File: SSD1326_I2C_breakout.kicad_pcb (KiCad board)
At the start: 2 copper layers, 55.9 x 12.8 mm, 24 parts, among them J1 Conn_01x04, U1 MAX607ESA-T, U2 ER-OLED018-1, U3 APX803, U4 AP2112K-3.3

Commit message: adding images and such
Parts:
- removed REF**: ER-OLED018-1_screen, onigaku:ER-OLED018-1_screen
- J1: footprint Connector_PinSocket_2.54mm:PinSocket_1x04_P2.54mm_Vertical -> onigaku:PinSocket_1x04_P2.54mm_Vertical
- renumbered Ce to C8
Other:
- board size 55.9 x 12.8 mm -> 55.7 x 12.8 mm

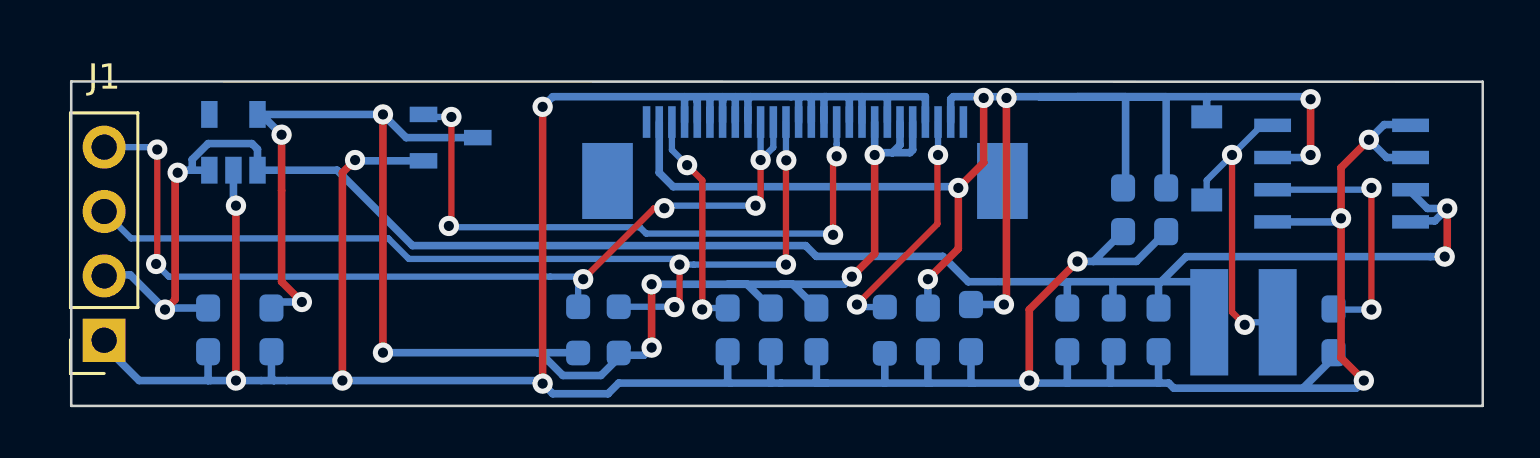
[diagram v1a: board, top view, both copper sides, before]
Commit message: swapped out max607 for a max8570 due to cost savings and obsoletion, using B0520LW schottky due to similar circumstances
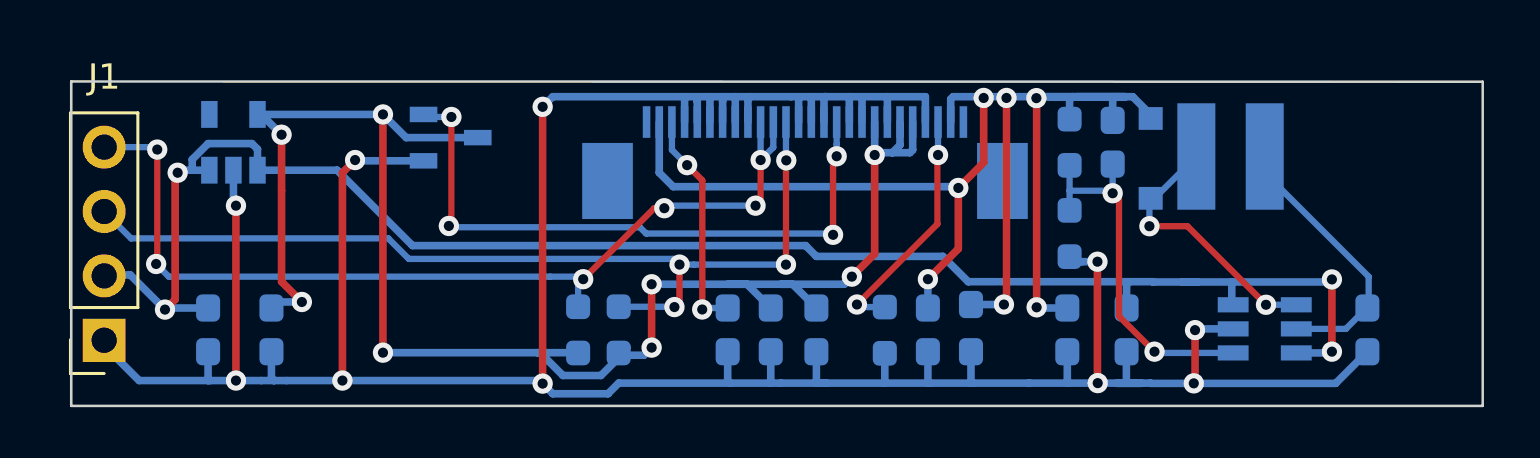
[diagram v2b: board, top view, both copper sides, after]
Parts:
- removed C4: 0.68uF, Capacitor_SMD:C_0603_1608Metric_Pad1.08x0.95mm_HandSolder
- removed C6: 10n, Capacitor_SMD:C_0603_1608Metric_Pad1.08x0.95mm_HandSolder
- removed U1: MAX607ESA-T, onigaku:max607esa&plus_T
- added R4: 88k, Resistor_SMD:R_0603_1608Metric_Pad0.98x0.95mm_HandSolder, B.Cu at (108.2, 30.1)
- added R5: 10k, Resistor_SMD:R_0603_1608Metric_Pad0.98x0.95mm_HandSolder, B.Cu at (108.2, 33.7)
- added U5: MAX8570EUT, onigaku:MAX8570EUT+SOT95P280X145-6N, B.Cu at (115.9, 37.5)
- C1: value 0.68uF -> 4.7uF
- C2: value 0.68uF -> 10pF
- C5: value 0.68uF -> 1uF
- D1: value MBR0520LT1G -> ‎B0520LW-7-F‎; footprint onigaku:MBR0520LT1G -> onigaku:B0520LW
- moved C1 9.25 mm to (120.0, 37.5)
- moved L1 6.56 mm to (114.5, 30.6), turned to 180 degrees
- moved C2 2.70 mm to (109.9, 30.1)
- moved D1 2.21 mm to (111.4, 30.7)
- moved C5 1.26 mm to (110.5, 37.5)
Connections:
- C1 pad 1: +12V -> Net-(C1-Pad1)
- C2 pad 2: GND -> Net-(C2-Pad2)
- C3 pad 1: +5V -> +12V
- L1 pad 1: +5V -> Net-(C1-Pad1)
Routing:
- net GND: track 153.3 -> 133.6 mm, vias 11 -> 10
- net Net-(C2-Pad2): track 0.00 -> 14.6 mm, vias 0 -> 2
- net Net-(C1-Pad1): track 0.00 -> 11.3 mm
- net Net-(C6-Pad1): track 10.2 -> 0.00 mm, vias 2 -> 0
- net +5V: track 76.1 -> 67.5 mm
- net +12V: track 66.6 -> 58.7 mm
- net Net-(D1-Pad2): track 12.5 -> 10.7 mm

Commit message: slimming down to 12mm
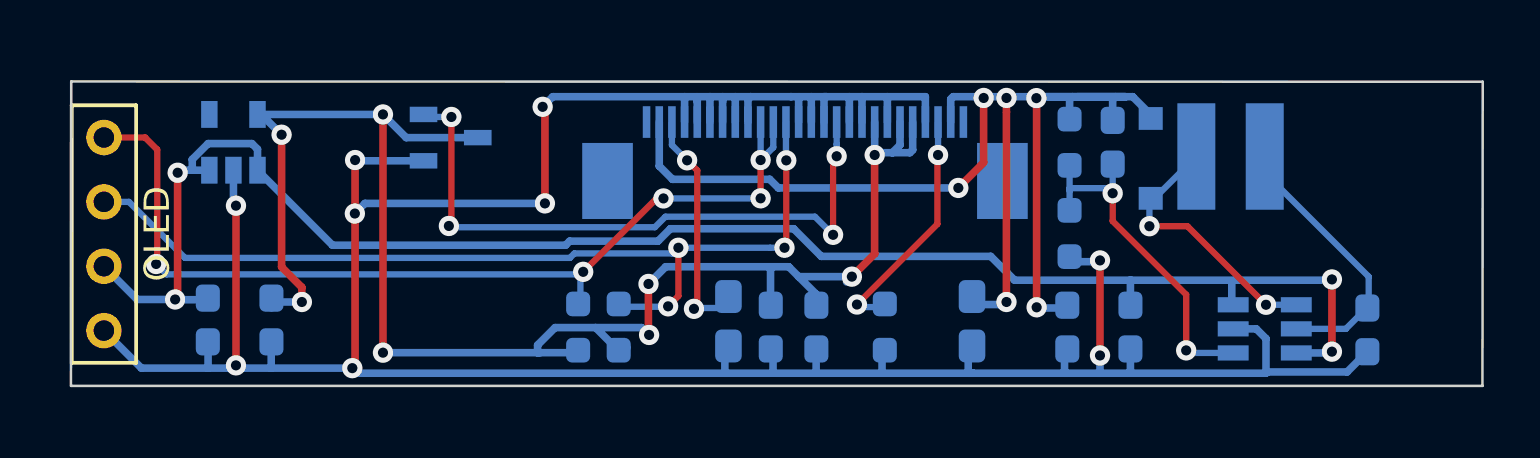
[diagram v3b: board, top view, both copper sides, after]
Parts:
- removed C7, C9: 4.7uF, Capacitor_SMD:C_0603_1608Metric_Pad1.08x0.95mm_HandSolder
- removed C8: 0.1uF, Capacitor_SMD:C_0603_1608Metric_Pad1.08x0.95mm_HandSolder
- added C4: 4.7uF, Capacitor_Tantalum_SMD:CP_EIA-2012-15_AVX-P_Pad1.30x1.05mm_HandSolder, B.Cu at (104.3, 37.1)
- added C6: 4.7uF, Capacitor_Tantalum_SMD:CP_EIA-2012-15_AVX-P_Pad1.30x1.05mm_HandSolder, B.Cu at (94.7, 37.1)
- C10: value 4.7uF -> 0.1uF
- J1: footprint onigaku:PinSocket_1x04_P2.54mm_Vertical -> kbd:OLED
- R4: value 88k -> 82k
- U3: value APX803 -> APX803S; footprint onigaku:APX803-SOT91P240X110-3N -> onigaku:APX803S-SA-SOT91P240X110-3N
- moved C12 0.39 mm to (74.2, 37.1)
- moved C13 0.39 mm to (76.7, 37.1)
- moved J1 0.38 mm to (70.1, 29.9), turned to 270 degrees
- moved C5 0.19 mm to (110.6, 37.4)
- moved R3 0.12 mm to (100.9, 37.4)
- moved C10 0.11 mm to (98.2, 37.4)
- moved C11 0.11 mm to (96.4, 37.4)
- moved C3 0.11 mm to (108.1, 37.4)
- moved R1 0.11 mm to (90.4, 37.4)
- moved R2 0.11 mm to (88.8, 37.4)
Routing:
- net GND: track 133.6 -> 127.2 mm, vias 10 -> 9
- net +12V: track 58.7 -> 53.3 mm, vias 7 -> 6
- net +3V3: track 66.7 -> 67.8 mm
- net Net-(C2-Pad2): track 14.6 -> 13.9 mm
- net SDA: track 38.1 -> 38.6 mm, vias 6 -> 5
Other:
- board size 55.7 x 12.8 mm -> 55.7 x 12 mm

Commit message: moved some stuff over
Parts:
- removed J1: Conn_01x04, kbd:OLED
- added Jee: Conn_01x04, kbd:OLED, F.Cu at (69.3, 29.9)
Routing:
- net SCL: track 37.4 -> 38.1 mm
- net +5V: track 67.0 -> 67.6 mm
- net GND: track 127.2 -> 127.8 mm
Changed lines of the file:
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@@
     (thickness 1.6)
     (drawings 6)
-    (tracks 353)
+    (tracks 354)
     (zones 0)
     (modules 22)
@@
   )
   (module kbd:OLED (layer F.Cu)
-    (at 70.1 29.9 270)
+    (at 69.35 29.9 270)
     (descr "Connecteur 6 pins")
     (tags "CONN DEV")
-    (fp_text reference J1 (at 3.7 2.1 270) (layer F.Fab)
+    (fp_text reference Jee (at 3.7 2.1 270) (layer F.Fab)
       (effects (font (size 0.8128 0.8128) (thickness 0.15)))
     )
     (fp_text value Conn_01x04 (at 3.6 3.3 90) (layer F.SilkS) hide
       (effects (font (size 0.8128 0.8128) (thickness 0.15)))
-    )
-    (fp_text user OLED (at 3.75 -2.1 90) (layer B.SilkS)
-      (effects (font (size 1 1) (thickness 0.15)) (justify mirror))
-    )
-    (fp_text user OLED (at 3.8 -2.1 90) (layer F.SilkS)
-      (effects (font (size 1 1) (thickness 0.15)))
     )
     (fp_line (start -1.27 -1.27) (end 8.89 -1.27) (layer B.SilkS) (width 0.15))
@@
     (fp_line (start 8.89 -1.27) (end 8.89 1.27) (layer F.SilkS) (width 0.15))
     (fp_line (start -1.27 1.27) (end -1.27 -1.27) (layer F.SilkS) (width 0.15))
+    (fp_text user OLED (at 3.75 -2.1 90) (layer B.SilkS)
+      (effects (font (size 1 1) (thickness 0.15)) (justify mirror))
+    )
+    (fp_text user OLED (at 3.8 -2.1 90) (layer F.SilkS)
+      (effects (font (size 1 1) (thickness 0.15)))
+    )
     (pad 4 thru_hole circle (at 7.62 0 270) (size 1.397 1.397) (drill 0.8128) (layers *.Cu *.Mask F.SilkS)
       (net 1 GND))
@@
     )
   )
-  (dimension 55.69 (width 0.15) (layer Dwgs.User)
-    (gr_text "55.690 mm" (at 96.655 25.2) (layer Dwgs.User)
+  (dimension 26 (width 0.15) (layer Dwgs.User)
+    (gr_text "26.000 mm" (at 84.75 24.85) (layer Dwgs.User)
       (effects (font (size 1 1) (thickness 0.15)))
     )
-    (feature1 (pts (xy 124.5 27.69) (xy 124.5 25.913579)))
-    (feature2 (pts (xy 68.81 27.69) (xy 68.81 25.913579)))
-    (crossbar (pts (xy 68.81 26.5) (xy 124.5 26.5)))
-    (arrow1a (pts (xy 124.5 26.5) (xy 123.373496 27.086421)))
-    (arrow1b (pts (xy 124.5 26.5) (xy 123.373496 25.913579)))
-    (arrow2a (pts (xy 68.81 26.5) (xy 69.936504 27.086421)))
-    (arrow2b (pts (xy 68.81 26.5) (xy 69.936504 25.913579)))
-  )
-  (dimension 12 (width 0.15) (layer Dwgs.User)
-    (gr_text "12.000 mm" (at 62.3 33.69 270) (layer Dwgs.User)
+    (feature1 (pts (xy 97.75 27.7) (xy 97.75 25.563579)))
+    (feature2 (pts (xy 71.75 27.7) (xy 71.75 25.563579)))
+    (crossbar (pts (xy 71.75 26.15) (xy 97.75 26.15)))
+    (arrow1a (pts (xy 97.75 26.15) (xy 96.623496 26.736421)))
+    (arrow1b (pts (xy 97.75 26.15) (xy 96.623496 25.563579)))
+    (arrow2a (pts (xy 71.75 26.15) (xy 72.876504 26.736421)))
+    (arrow2b (pts (xy 71.75 26.15) (xy 72.876504 25.563579)))
+  )
+  (dimension 52 (width 0.15) (layer Dwgs.User)
+    (gr_text "52.000 mm" (at 97.75 21.000001) (layer Dwgs.User)
       (effects (font (size 1 1) (thickness 0.15)))
     )
-    (feature1 (pts (xy 68.81 39.69) (xy 63.013579 39.69)))
-    (feature2 (pts (xy 68.81 27.69) (xy 63.013579 27.69)))
-    (crossbar (pts (xy 63.6 27.69) (xy 63.6 39.69)))
-    (arrow1a (pts (xy 63.6 39.69) (xy 63.013579 38.563496)))
-    (arrow1b (pts (xy 63.6 39.69) (xy 64.186421 38.563496)))
-    (arrow2a (pts (xy 63.6 27.69) (xy 63.013579 28.816504)))
-    (arrow2b (pts (xy 63.6 27.69) (xy 64.186421 28.816504)))
-  )
-  (gr_line (start 124.5 27.7) (end 68.81 27.69) (layer Edge.Cuts) (width 0.1))
-  (gr_line (start 124.49 39.7) (end 124.5 27.7) (layer Edge.Cuts) (width 0.1))
-  (gr_line (start 68.8 39.7) (end 124.49 39.7) (layer Edge.Cuts) (width 0.1))
-  (gr_line (start 68.81 27.69) (end 68.8 39.7) (layer Edge.Cuts) (width 0.1))
+    (feature1 (pts (xy 71.75 27.7) (xy 71.75 21.71358)))
+    (feature2 (pts (xy 123.75 27.7) (xy 123.75 21.71358)))
+    (crossbar (pts (xy 123.75 22.300001) (xy 71.75 22.300001)))
+    (arrow1a (pts (xy 71.75 22.300001) (xy 72.876504 21.71358)))
+    (arrow1b (pts (xy 71.75 22.300001) (xy 72.876504 22.886422)))
+    (arrow2a (pts (xy 123.75 22.300001) (xy 122.623496 21.71358)))
+    (arrow2b (pts (xy 123.75 22.300001) (xy 122.623496 22.886422)))
+  )
+  (gr_line (start 123.75 27.7) (end 68.06 27.69) (layer Edge.Cuts) (width 0.1))
+  (gr_line (start 123.74 39.7) (end 123.75 27.7) (layer Edge.Cuts) (width 0.1))
+  (gr_line (start 68.05 39.7) (end 123.74 39.7) (layer Edge.Cuts) (width 0.1))
+  (gr_line (start 68.06 27.69) (end 68.05 39.7) (layer Edge.Cuts) (width 0.1))
   (via (at 80.01 30.79) (size 0.8) (drill 0.4) (layers F.Cu B.Cu) (net 1))
   (segment (start 80.04 30.82) (end 80.01 30.79) (width 0.3) (layer B.Cu) (net 1))
@@
   (segment (start 76.7 39) (end 76.7 37.9725) (width 0.3) (layer B.Cu) (net 1))
   (segment (start 74.21 38.3525) (end 74.21 39) (width 0.3) (layer B.Cu) (net 1))
-  (segment (start 71.58 39) (end 74.21 39) (width 0.3) (layer B.Cu) (net 1))
-  (segment (start 70.1 37.52) (end 71.58 39) (width 0.3) (layer B.Cu) (net 1))
   (via (at 75.31 38.89) (size 0.8) (drill 0.4) (layers F.Cu B.Cu) (net 1))
   (segment (start 75.2 39) (end 75.31 38.89) (width 0.3) (layer B.Cu) (net 1))
@@
   (segment (start 110.6 39.2) (end 110.6 38.4125) (width 0.3) (layer B.Cu) (net 1))
   (segment (start 109.3 39.2) (end 110.5 39.2) (width 0.3) (layer B.Cu) (net 1))
+  (segment (start 71.58 39) (end 74.21 39) (width 0.3) (layer B.Cu) (net 1))
+  (segment (start 69.35 37.52) (end 71.58 39) (width 0.3) (layer B.Cu) (net 1))
   (segment (start 103.51 28.384998) (end 103.51 29.29) (width 0.3) (layer B.Cu) (net 2))
   (segment (start 103.604998 28.29) (end 103.51 28.384998) (width 0.3) (layer B.Cu) (net 2))
@@
   (via (at 72.909992 36.290008) (size 0.8) (drill 0.4) (layers F.Cu B.Cu) (net 3))
   (segment (start 73.01 31.29) (end 73.01 36.19) (width 0.3) (layer F.Cu) (net 3))
-  (segment (start 70.1 34.98) (end 71.410008 36.290008) (width 0.3) (layer B.Cu) (net 3))
   (segment (start 73.01 36.19) (end 72.909992 36.290008) (width 0.3) (layer F.Cu) (net 3))
-  (segment (start 71.410008 36.290008) (end 72.909992 36.290008) (width 0.3) (layer B.Cu) (net 3))
   (segment (start 72.919984 36.3) (end 72.909992 36.290008) (width 0.3) (layer B.Cu) (net 3))
   (segment (start 74.2 36.3) (end 72.919984 36.3) (width 0.3) (layer B.Cu) (net 3))
   (segment (start 74.3 36.2) (end 74.2 36.3) (width 0.3) (layer B.Cu) (net 3))
+  (segment (start 71.410008 36.290008) (end 72.909992 36.290008) (width 0.3) (layer B.Cu) (net 3))
+  (segment (start 69.35 34.98) (end 71.410008 36.290008) (width 0.3) (layer B.Cu) (net 3))
   (segment (start 76.31 28.99) (end 77.11 29.79) (width 0.3) (layer B.Cu) (net 4))
   (segment (start 76.16 28.99) (end 76.31 28.99) (width 0.3) (layer B.Cu) (net 4))
@@
   (segment (start 92.539981 34.474999) (end 92.76499 34.24999) (width 0.25) (layer B.Cu) (net 6))
   (segment (start 88.487009 34.649989) (end 88.661999 34.474999) (width 0.25) (layer B.Cu) (net 6))
+  (segment (start 70.1 32.44) (end 69.35 32.44) (width 0.25) (layer B.Cu) (net 6))
   (via (at 72.16 34.89) (size 0.8) (drill 0.4) (layers F.Cu B.Cu) (net 7))
   (segment (start 96.51 29.29) (end 96.51 30.29) (width 0.25) (layer B.Cu) (net 7))
@@
   (segment (start 96.51 30.29) (end 96.01 30.79) (width 0.25) (layer B.Cu) (net 7))
   (via (at 96.01 30.79) (size 0.8) (drill 0.4) (layers F.Cu B.Cu) (net 7))
-  (segment (start 70.11 30.49) (end 70.32 30.28) (width 0.25) (layer B.Cu) (net 7))
   (segment (start 72.203857 34.846143) (end 72.16 34.89) (width 0.25) (layer F.Cu) (net 7))
   (segment (start 72.203857 30.376177) (end 72.203857 34.846143) (width 0.25) (layer F.Cu) (net 7))
@@
   (segment (start 88.9 36.4875) (end 88.9 35.31) (width 0.25) (layer B.Cu) (net 7))
   (segment (start 88.81 36.5775) (end 88.9 36.4875) (width 0.25) (layer B.Cu) (net 7))
+  (segment (start 70.1 29.9) (end 69.35 29.9) (width 0.25) (layer F.Cu) (net 7))
   (via (at 99.81 36.49) (size 0.8) (drill 0.4) (layers F.Cu B.Cu) (net 8))
   (segment (start 99.91 36.59) (end 99.81 36.49) (width 0.25) (layer B.Cu) (net 8))
